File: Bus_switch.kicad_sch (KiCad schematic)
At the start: 15 parts, among them J3 Conn_01x04_Pin, U1 SN74CB3Q3384APW

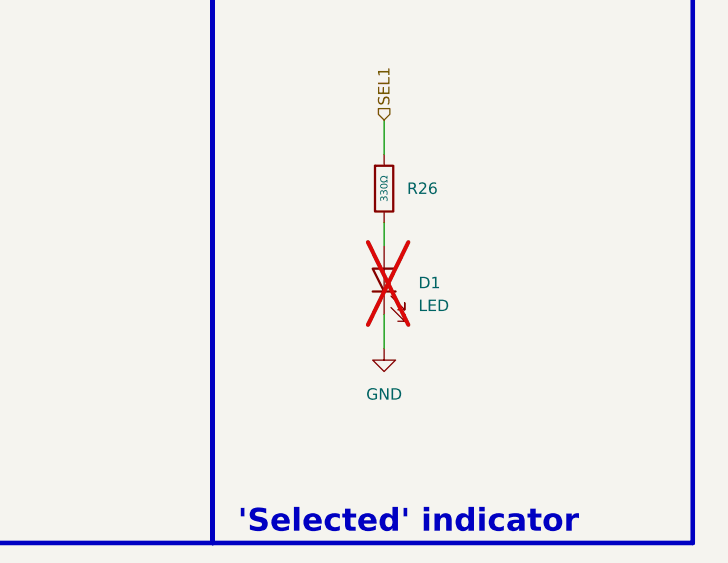
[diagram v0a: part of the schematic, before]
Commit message: changed diode to JLCMANUFACTURING
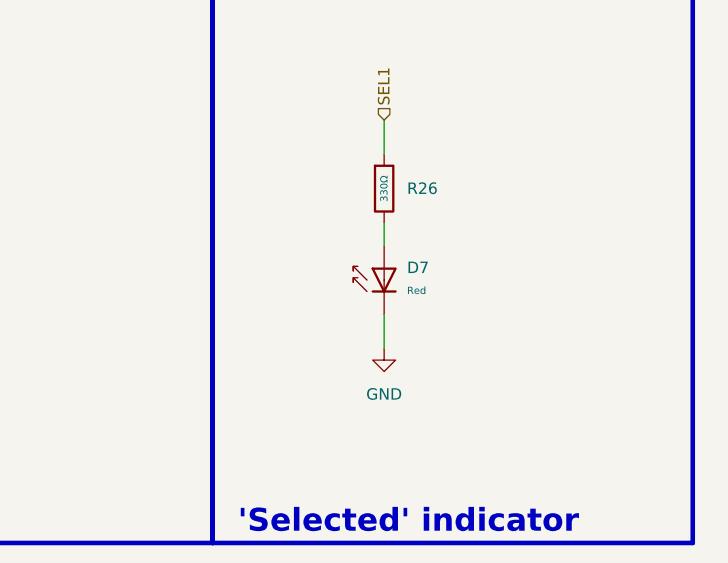
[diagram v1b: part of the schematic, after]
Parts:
- removed D1: LED, LED_SMD:LED_0603_1608Metric, symbol Device:LED
- added D7: Red, PCM_JLCPCB:D_0603, symbol PCM_JLCPCB-Diodes:LED,0603,Red
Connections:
- net GND: now also D7.1
- net at R26.2: now also D7.2
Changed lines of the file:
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@@
-	)
-	(symbol
-		(lib_id "Device:LED")
-		(at 246.38 124.46 90)
-		(unit 1)
-		(exclude_from_sim no)
-		(in_bom yes)
-		(on_board yes)
-		(dnp yes)
-		(fields_autoplaced yes)
-		(property "Reference" "D1"
-			(at 250.19 124.7774 90)
-			(effects
-				(font
-					(size 1.27 1.27)
-				)
-				(justify right)
-			)
-		)
-		(property "Value" "LED"
-			(at 250.19 127.3174 90)
-			(effects
-				(font
-					(size 1.27 1.27)
-				)
-				(justify right)
-			)
-		)
-		(property "Footprint" "LED_SMD:LED_0603_1608Metric"
-			(at 246.38 124.46 0)
-			(effects
-				(font
-					(size 1.27 1.27)
-				)
-				(hide yes)
-			)
-		)
-		(property "Datasheet" "~"
-			(at 246.38 124.46 0)
-			(effects
-				(font
-					(size 1.27 1.27)
-				)
-				(hide yes)
-			)
-		)
-		(property "Description" "Light emitting diode"
-			(at 246.38 124.46 0)
-			(effects
-				(font
-					(size 1.27 1.27)
-				)
-				(hide yes)
-			)
-		)
-		(property "Sim.Pins" "1=K 2=A"
-			(at 246.38 124.46 0)
-			(effects
-				(font
-					(size 1.27 1.27)
-				)
-				(hide yes)
-			)
-		)
-		(property "Sim.Device" ""
-			(at 246.38 124.46 90)
-			(effects
-				(font
-					(size 1.27 1.27)
-				)
-				(hide yes)
-			)
-		)
-		(pin "2"
-		)
-		(pin "1"
-		)
-		(instances
-			(project ""
-				(path "/6596548a-44e0-46d8-8624-fd71cf4a3e17/ec6d73af-72b0-4068-85fb-cca3c5143749"
-					(reference "D1")
-					(unit 1)
-				)
-			)
-		)
 	)
 	(symbol
@@
 					(unit 1)
 				)
+			)
+		)
+	)
+	(symbol
+		(lib_id "PCM_JLCPCB-Diodes:LED,0603,Red")
+		(at 246.38 124.46 0)
+		(unit 1)
+		(exclude_from_sim no)
+		(in_bom yes)
+		(on_board yes)
+		(dnp no)
+		(fields_autoplaced yes)
+		(property "Reference" "D7"
+			(at 248.92 123.0946 0)
+			(effects
+				(font
+					(size 1.27 1.27)
+				)
+				(justify left)
+			)
+		)
+		(property "Value" "Red"
+			(at 248.92 125.6347 0)
+			(effects
+				(font
+					(size 0.8 0.8)
+				)
+				(justify left)
+			)
+		)
+		(property "Footprint" "PCM_JLCPCB:D_0603"
+			(at 244.602 124.46 90)
+			(effects
+				(font
+					(size 1.27 1.27)
+				)
+				(hide yes)
+			)
+		)
+		(property "Datasheet" "https://www.lcsc.com/datasheet/lcsc_datasheet_1810231112_Hubei-KENTO-Elec-KT-0603R_C2286.pdf"
+			(at 246.38 124.46 0)
+			(effects
+				(font
+					(size 1.27 1.27)
+				)
+				(hide yes)
+			)
+		)
+		(property "Description" "-40°C~+85°C Red 0603 LED Indication - Discrete ROHS"
+			(at 246.38 124.46 0)
+			(effects
+				(font
+					(size 1.27 1.27)
+				)
+				(hide yes)
+			)
+		)
+		(property "LCSC" "C2286"
+			(at 246.38 124.46 0)
+			(effects
+				(font
+					(size 1.27 1.27)
+				)
+				(hide yes)
+			)
+		)
+		(property "Stock" "5373336"
+			(at 246.38 124.46 0)
+			(effects
+				(font
+					(size 1.27 1.27)
+				)
+				(hide yes)
+			)
+		)
+		(property "Price" "0.009USD"
+			(at 246.38 124.46 0)
+			(effects
+				(font
+					(size 1.27 1.27)
+				)
+				(hide yes)
+			)
+		)
+		(property "Process" "SMT"
+			(at 246.38 124.46 0)
+			(effects
+				(font
+					(size 1.27 1.27)
+				)
+				(hide yes)
+			)
+		)
+		(property "Minimum Qty" "20"
+			(at 246.38 124.46 0)
+			(effects
+				(font
+					(size 1.27 1.27)
+				)
+				(hide yes)
+			)
+		)
+		(property "Attrition Qty" "10"
+			(at 246.38 124.46 0)
+			(effects
+				(font
+					(size 1.27 1.27)
+				)
+				(hide yes)
+			)
+		)
+		(property "Class" "Basic Component"
+			(at 246.38 124.46 0)
+			(effects
+				(font
+					(size 1.27 1.27)
+				)
+				(hide yes)
+			)
+		)
+		(property "Category" "Optocouplers & LEDs & Infrared,Light Emitting Diodes (LED)"
+			(at 246.38 124.46 0)
+			(effects
+				(font
+					(size 1.27 1.27)
+				)
+				(hide yes)
+			)
+		)
+		(property "Manufacturer" "Hubei KENTO Elec"
+			(at 246.38 124.46 0)
+			(effects
+				(font
+					(size 1.27 1.27)
+				)
+				(hide yes)
+			)
+		)
+		(property "Part" "KT-0603R"
+			(at 246.38 124.46 0)
+			(effects
+				(font
+					(size 1.27 1.27)
+				)
+				(hide yes)
+			)
+		)
+		(pin "2"
+		)
+		(pin "1"
+		)
+		(instances
+			(project ""
+				(path "/6596548a-44e0-46d8-8624-fd71cf4a3e17/ec6d73af-72b0-4068-85fb-cca3c5143749"
+					(reference "D7")
+					(unit 1)
+				)
